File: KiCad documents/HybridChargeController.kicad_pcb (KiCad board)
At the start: 2 copper layers, 87 x 87 mm, 103 parts, among them P1 Load, P2 LI_balancer, P3 PV, P4 Extra, P5 LI, P6 LA, Q1 MMBT3904, Q10 MMBT3904, Q11 IPD90P04P4L-04, Q12 STL60P4LLF6, Q13 STL60P4LLF6, Q14 IPD90P04P4L-04, Q15 BSS138, Q16 BSS138, Q2 IPD90P04P4L-04, Q3 MMBT3904, Q4 IPD90P04P4L-04, Q5 IPD90P04P4L-04, Q6 MMBT3904, Q7 MMBT3904, Q8 MMBT3904, Q9 IPD90P04P4L-04, U1 LM358D, U2 bq76920, U3 cd4051, U4 LM358D, U5 LM358D

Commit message: switched 8 and 9 and hope for the best
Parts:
- added P7: FTDI, Pin_Headers:Pin_Header_Straight_1x06_Pitch2.54mm, F.Cu at (143.5, 137.1)
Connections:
- AU1 pad 8: /SW_PV -> /Alert
- AU1 pad 9: /Alert -> /SW_PV
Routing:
- net /SW_PV: track 15.1 -> 19.1 mm, vias 2 -> 3
- net /Alert: track 66.7 -> 70.2 mm, vias 5 -> 6
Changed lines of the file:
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@@
 (kicad_pcb (version 4) (host pcbnew 4.0.4-stable)
   (general
-    (links 252)
-    (no_connects 2)
-    (area 97 39 189.000001 129.000001)
+    (links 258)
+    (no_connects 8)
+    (area 99.924999 39.924999 187.075001 127.075001)
     (thickness 1.6)
     (drawings 58)
-    (tracks 882)
+    (tracks 893)
     (zones 0)
-    (modules 103)
+    (modules 104)
     (nets 92)
   )
@@
       (net 15 /SW_LD))
     (pad 8 thru_hole circle (at 41.656 -50.8 90) (size 1.7 1.7) (drill 1) (layers *.Cu *.Mask F.SilkS)
-      (net 68 /SW_PV))
-    (pad 9 thru_hole circle (at 39.116 -50.8 90) (size 1.7 1.7) (drill 1) (layers *.Cu *.Mask F.SilkS)
       (net 76 /Alert))
+    (pad 9 thru_hole circle (at 39.116 -50.8 90) (size 1.7 1.7) (drill 1) (layers *.Cu *.Mask F.SilkS)
+      (net 68 /SW_PV))
     (pad 10 thru_hole circle (at 36.576 -50.8 90) (size 1.7 1.7) (drill 1) (layers *.Cu *.Mask F.SilkS)
       (net 16 /SS))
@@
     )
   )
+  (module Pin_Headers:Pin_Header_Straight_1x06_Pitch2.54mm (layer F.Cu)
+    (at 143.5 137.075001)
+    (descr "Through hole straight pin header, 1x06, 2.54mm pitch, single row")
+    (tags "Through hole pin header THT 1x06 2.54mm single row")
+    (fp_text reference P7 (at 0 -2.33) (layer F.SilkS)
+      (effects (font (size 1 1) (thickness 0.15)))
+    )
+    (fp_text value FTDI (at 0 15.03) (layer F.Fab)
+      (effects (font (size 1 1) (thickness 0.15)))
+    )
+    (fp_line (start -1.27 -1.27) (end -1.27 13.97) (layer F.Fab) (width 0.1))
+    (fp_line (start -1.27 13.97) (end 1.27 13.97) (layer F.Fab) (width 0.1))
+    (fp_line (start 1.27 13.97) (end 1.27 -1.27) (layer F.Fab) (width 0.1))
+    (fp_line (start 1.27 -1.27) (end -1.27 -1.27) (layer F.Fab) (width 0.1))
+    (fp_line (start -1.33 1.27) (end -1.33 14.03) (layer F.SilkS) (width 0.12))
+    (fp_line (start -1.33 14.03) (end 1.33 14.03) (layer F.SilkS) (width 0.12))
+    (fp_line (start 1.33 14.03) (end 1.33 1.27) (layer F.SilkS) (width 0.12))
+    (fp_line (start 1.33 1.27) (end -1.33 1.27) (layer F.SilkS) (width 0.12))
+    (fp_line (start -1.33 0) (end -1.33 -1.33) (layer F.SilkS) (width 0.12))
+    (fp_line (start -1.33 -1.33) (end 0 -1.33) (layer F.SilkS) (width 0.12))
+    (fp_line (start -1.8 -1.8) (end -1.8 14.5) (layer F.CrtYd) (width 0.05))
+    (fp_line (start -1.8 14.5) (end 1.8 14.5) (layer F.CrtYd) (width 0.05))
+    (fp_line (start 1.8 14.5) (end 1.8 -1.8) (layer F.CrtYd) (width 0.05))
+    (fp_line (start 1.8 -1.8) (end -1.8 -1.8) (layer F.CrtYd) (width 0.05))
+    (fp_text user %R (at 0 -2.33) (layer F.Fab)
+      (effects (font (size 1 1) (thickness 0.15)))
+    )
+    (pad 1 thru_hole rect (at 0 0) (size 1.7 1.7) (drill 1) (layers *.Cu *.Mask)
+      (net 90 "Net-(P7-Pad1)"))
+    (pad 2 thru_hole oval (at 0 2.54) (size 1.7 1.7) (drill 1) (layers *.Cu *.Mask)
+      (net 9 /TX))
+    (pad 3 thru_hole oval (at 0 5.08) (size 1.7 1.7) (drill 1) (layers *.Cu *.Mask)
+      (net 8 /RX))
+    (pad 4 thru_hole oval (at 0 7.62) (size 1.7 1.7) (drill 1) (layers *.Cu *.Mask)
+      (net 21 /5V))
+    (pad 5 thru_hole oval (at 0 10.16) (size 1.7 1.7) (drill 1) (layers *.Cu *.Mask)
+      (net 91 "Net-(P7-Pad5)"))
+    (pad 6 thru_hole oval (at 0 12.7) (size 1.7 1.7) (drill 1) (layers *.Cu *.Mask)
+      (net 6 /GND))
+    (model ${KISYS3DMOD}/Pin_Headers.3dshapes/Pin_Header_Straight_1x06_Pitch2.54mm.wrl
+      (at (xyz 0 -0.25 0))
+      (scale (xyz 1 1 1))
+      (rotate (xyz 0 0 90))
+    )
+  )
   (gr_text X (at 176.25 79 90) (layer F.SilkS)
     (effects (font (size 0.75 0.75) (thickness 0.1)))
@@
   (segment (start 108.75 60.25) (end 109.365 59.635) (width 0.25) (layer F.Cu) (net 67))
   (segment (start 109.365 59.635) (end 109.365 58.825) (width 0.25) (layer F.Cu) (net 67))
-  (segment (start 165.1 71) (end 165 71) (width 0.25) (layer F.Cu) (net 68))
-  (segment (start 165 71) (end 164.25 71.75) (width 0.25) (layer F.Cu) (net 68))
-  (via (at 164.25 71.75) (size 0.6) (drill 0.4) (layers F.Cu B.Cu) (net 68))
-  (segment (start 164.25 71.75) (end 163.25 72.75) (width 0.25) (layer B.Cu) (net 68))
-  (segment (start 163.25 72.75) (end 163.25 73.25) (width 0.25) (layer B.Cu) (net 68))
-  (via (at 163.25 73.25) (size 0.6) (drill 0.4) (layers F.Cu B.Cu) (net 68))
-  (segment (start 163.25 73.25) (end 163.25 75.25) (width 0.25) (layer F.Cu) (net 68))
-  (segment (start 163.25 75.25) (end 161.25 77.25) (width 0.25) (layer F.Cu) (net 68))
+  (segment (start 158.276 77.25) (end 158.25 77.25) (width 0.25) (layer F.Cu) (net 68))
   (segment (start 161.25 77.25) (end 158.276 77.25) (width 0.25) (layer F.Cu) (net 68))
-  (segment (start 158.276 77.25) (end 155.321 74.295) (width 0.25) (layer F.Cu) (net 68))
+  (segment (start 163.25 75.25) (end 161.25 77.25) (width 0.25) (layer F.Cu) (net 68))
+  (segment (start 163.25 73.25) (end 163.25 75.25) (width 0.25) (layer F.Cu) (net 68))
+  (via (at 163.25 73.25) (size 0.6) (drill 0.4) (layers F.Cu B.Cu) (net 68))
+  (segment (start 163.25 72.75) (end 163.25 73.25) (width 0.25) (layer B.Cu) (net 68))
+  (segment (start 164.25 71.75) (end 163.25 72.75) (width 0.25) (layer B.Cu) (net 68))
+  (via (at 164.25 71.75) (size 0.6) (drill 0.4) (layers F.Cu B.Cu) (net 68))
+  (segment (start 165 71) (end 164.25 71.75) (width 0.25) (layer F.Cu) (net 68))
+  (segment (start 152.781 75.581) (end 152.781 74.295) (width 0.25) (layer B.Cu) (net 68))
+  (segment (start 153.7 76.5) (end 152.781 75.581) (width 0.25) (layer B.Cu) (net 68))
+  (segment (start 154.8 76.5) (end 153.7 76.5) (width 0.25) (layer B.Cu) (net 68))
+  (segment (start 155.7 75.6) (end 154.8 76.5) (width 0.25) (layer B.Cu) (net 68))
+  (segment (start 156.3 75.6) (end 155.7 75.6) (width 0.25) (layer B.Cu) (net 68))
+  (via (at 156.3 75.6) (size 0.6) (drill 0.4) (layers F.Cu B.Cu) (net 68))
+  (segment (start 156.6 75.6) (end 156.3 75.6) (width 0.25) (layer F.Cu) (net 68))
+  (segment (start 158.25 77.25) (end 156.6 75.6) (width 0.25) (layer F.Cu) (net 68))
+  (segment (start 165.1 71) (end 165 71) (width 0.25) (layer F.Cu) (net 68))
   (segment (start 166.825 96.425) (end 166.825 87.175) (width 0.25) (layer F.Cu) (net 69))
   (segment (start 169.5 68.75) (end 169.1 68.35) (width 0.25) (layer F.Cu) (net 69))
@@
   (segment (start 182.175 67.615) (end 184.015 67.615) (width 0.25) (layer F.Cu) (net 73))
   (segment (start 184.015 67.615) (end 185.25 68.85) (width 0.25) (layer F.Cu) (net 73))
-  (segment (start 152.781 74.295) (end 152.781 76.469) (width 0.25) (layer B.Cu) (net 76))
-  (segment (start 133.5 105.25) (end 138 100.75) (width 0.25) (layer F.Cu) (net 76))
-  (segment (start 138 100.75) (end 138 89.75) (width 0.25) (layer F.Cu) (net 76))
-  (via (at 138 89.75) (size 0.6) (drill 0.4) (layers F.Cu B.Cu) (net 76))
-  (segment (start 138 89.75) (end 138 85.5) (width 0.25) (layer B.Cu) (net 76))
-  (via (at 138 85.5) (size 0.6) (drill 0.4) (layers F.Cu B.Cu) (net 76))
-  (segment (start 119.183 117.433) (end 119.183 116.721) (width 0.25) (layer F.Cu) (net 76))
-  (segment (start 125.5 108.75) (end 129 105.25) (width 0.25) (layer F.Cu) (net 76))
-  (via (at 125.5 108.75) (size 0.6) (drill 0.4) (layers F.Cu B.Cu) (net 76))
-  (segment (start 125.5 111.25) (end 125.5 108.75) (width 0.25) (layer B.Cu) (net 76))
-  (segment (start 119.25 117.5) (end 125.5 111.25) (width 0.25) (layer B.Cu) (net 76))
-  (via (at 119.25 117.5) (size 0.6) (drill 0.4) (layers F.Cu B.Cu) (net 76))
-  (segment (start 119.183 117.433) (end 119.25 117.5) (width 0.25) (layer F.Cu) (net 76))
+  (segment (start 152 77.25) (end 155.25 77.25) (width 0.25) (layer B.Cu) (net 76))
   (segment (start 129 105.25) (end 133.5 105.25) (width 0.25) (layer F.Cu) (net 76))
-  (segment (start 138 80.75) (end 138 85.5) (width 0.25) (layer F.Cu) (net 76))
-  (segment (start 141.5 77.25) (end 138 80.75) (width 0.25) (layer F.Cu) (net 76))
-  (segment (start 152 77.25) (end 141.5 77.25) (width 0.25) (layer F.Cu) (net 76))
+  (segment (start 119.183 117.433) (end 119.25 117.5) (width 0.25) (layer F.Cu) (net 76))
+  (via (at 119.25 117.5) (size 0.6) (drill 0.4) (layers F.Cu B.Cu) (net 76))
+  (segment (start 119.25 117.5) (end 125.5 111.25) (width 0.25) (layer B.Cu) (net 76))
+  (segment (start 125.5 111.25) (end 125.5 108.75) (width 0.25) (layer B.Cu) (net 76))
+  (via (at 125.5 108.75) (size 0.6) (drill 0.4) (layers F.Cu B.Cu) (net 76))
+  (segment (start 125.5 108.75) (end 129 105.25) (width 0.25) (layer F.Cu) (net 76))
+  (segment (start 119.183 116.721) (end 119.183 117.433) (width 0.25) (layer F.Cu) (net 76))
+  (via (at 138 85.5) (size 0.6) (drill 0.4) (layers F.Cu B.Cu) (net 76))
+  (segment (start 138 89.75) (end 138 85.5) (width 0.25) (layer B.Cu) (net 76))
+  (via (at 138 89.75) (size 0.6) (drill 0.4) (layers F.Cu B.Cu) (net 76))
+  (segment (start 138 100.75) (end 138 89.75) (width 0.25) (layer F.Cu) (net 76))
+  (segment (start 133.5 105.25) (end 138 100.75) (width 0.25) (layer F.Cu) (net 76))
   (via (at 152 77.25) (size 0.6) (drill 0.4) (layers F.Cu B.Cu) (net 76))
-  (segment (start 152.781 76.469) (end 152 77.25) (width 0.25) (layer B.Cu) (net 76))
+  (segment (start 152 77.25) (end 141.5 77.25) (width 0.25) (layer F.Cu) (net 76))
+  (segment (start 141.5 77.25) (end 138 80.75) (width 0.25) (layer F.Cu) (net 76))
+  (segment (start 138 80.75) (end 138 85.5) (width 0.25) (layer F.Cu) (net 76))
+  (segment (start 155.321 75.821) (end 155.321 74.295) (width 0.25) (layer F.Cu) (net 76))
+  (segment (start 156 76.5) (end 155.321 75.821) (width 0.25) (layer F.Cu) (net 76))
+  (via (at 156 76.5) (size 0.6) (drill 0.4) (layers F.Cu B.Cu) (net 76))
+  (segment (start 155.25 77.25) (end 156 76.5) (width 0.25) (layer B.Cu) (net 76))
   (segment (start 120.1 89.73) (end 120.1 94.2) (width 0.25) (layer F.Cu) (net 80))
   (segment (start 120.1 94.2) (end 124 98.1) (width 0.25) (layer F.Cu) (net 80))

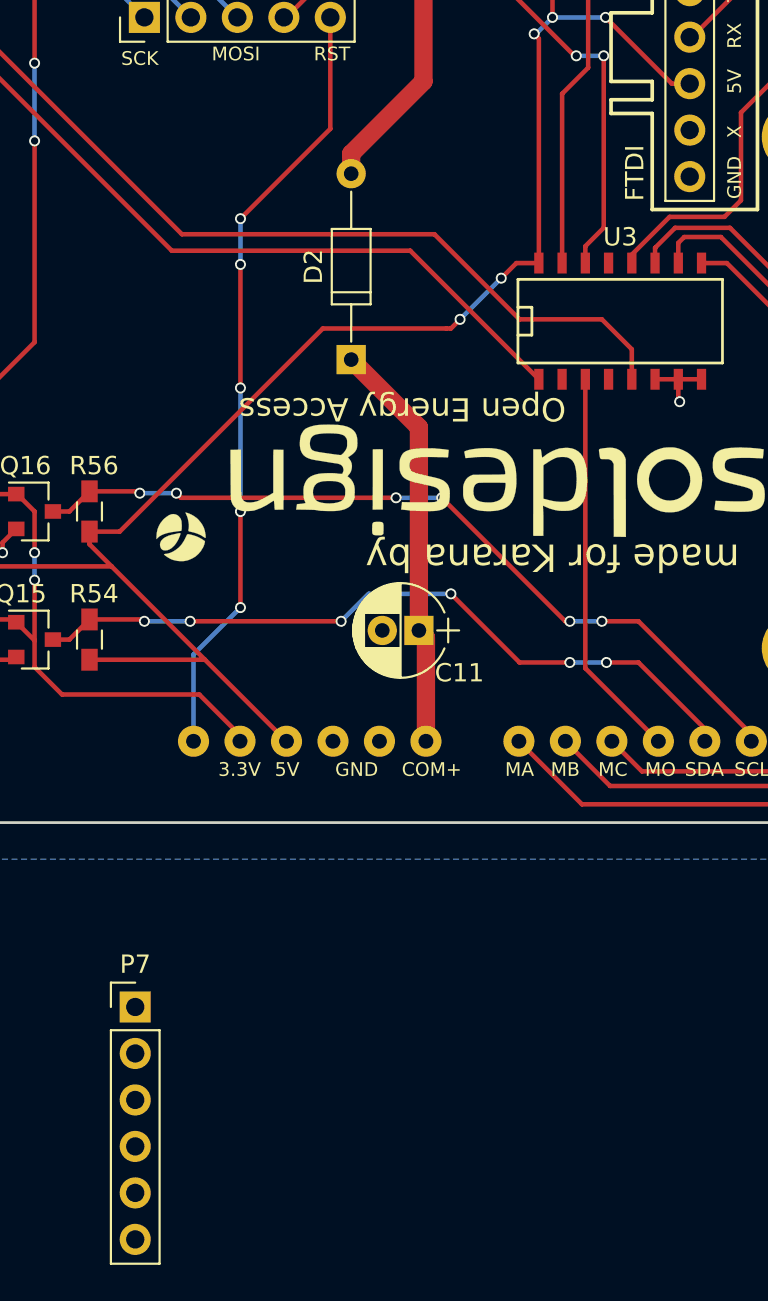
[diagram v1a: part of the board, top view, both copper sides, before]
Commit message: fixed extra holes, send new gerbers
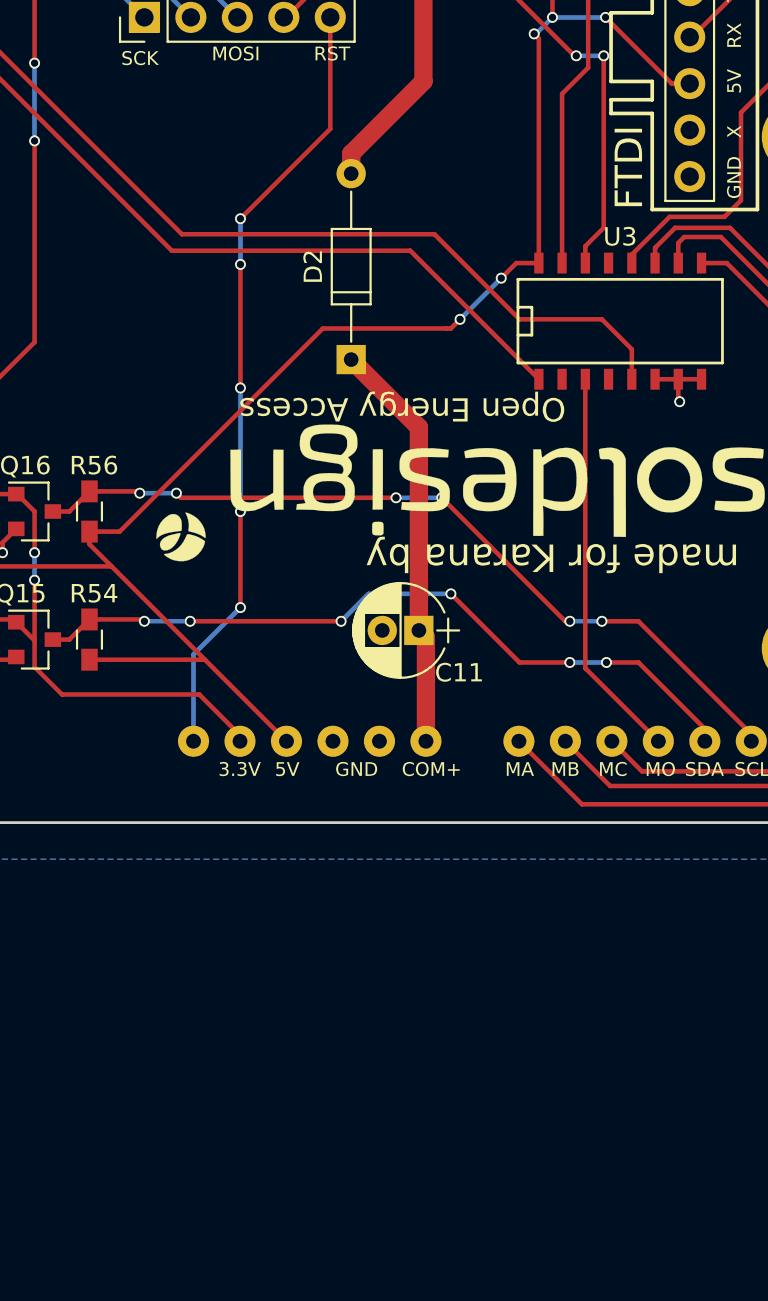
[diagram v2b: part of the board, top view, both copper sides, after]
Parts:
- removed the P7 at (143.5, 137.1)
- renumbered FTDI to P7
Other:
- board text added: "FTDI"
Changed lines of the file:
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@@
 (kicad_pcb (version 4) (host pcbnew 4.0.4-stable)
   (general
-    (links 258)
-    (no_connects 8)
+    (links 0)
+    (no_connects 2)
     (area 99.924999 39.924999 187.075001 127.075001)
     (thickness 1.6)
-    (drawings 58)
+    (drawings 59)
     (tracks 893)
     (zones 0)
-    (modules 104)
+    (modules 103)
     (nets 92)
   )
@@
     (descr "Through hole straight pin header, 1x06, 2.54mm pitch, single row")
     (tags "Through hole pin header THT 1x06 2.54mm single row")
-    (fp_text reference FTDI (at -3 12.5 90) (layer F.SilkS)
+    (fp_text reference P7 (at -3.1 2.3 90) (layer F.Fab)
       (effects (font (size 1 1) (thickness 0.15)))
     )
@@
     )
   )
-  (module Pin_Headers:Pin_Header_Straight_1x06_Pitch2.54mm (layer F.Cu)
-    (at 143.5 137.075001)
-    (descr "Through hole straight pin header, 1x06, 2.54mm pitch, single row")
-    (tags "Through hole pin header THT 1x06 2.54mm single row")
-    (fp_text reference P7 (at 0 -2.33) (layer F.SilkS)
-      (effects (font (size 1 1) (thickness 0.15)))
-    )
-    (fp_text value FTDI (at 0 15.03) (layer F.Fab)
-      (effects (font (size 1 1) (thickness 0.15)))
-    )
-    (fp_line (start -1.27 -1.27) (end -1.27 13.97) (layer F.Fab) (width 0.1))
-    (fp_line (start -1.27 13.97) (end 1.27 13.97) (layer F.Fab) (width 0.1))
-    (fp_line (start 1.27 13.97) (end 1.27 -1.27) (layer F.Fab) (width 0.1))
-    (fp_line (start 1.27 -1.27) (end -1.27 -1.27) (layer F.Fab) (width 0.1))
-    (fp_line (start -1.33 1.27) (end -1.33 14.03) (layer F.SilkS) (width 0.12))
-    (fp_line (start -1.33 14.03) (end 1.33 14.03) (layer F.SilkS) (width 0.12))
-    (fp_line (start 1.33 14.03) (end 1.33 1.27) (layer F.SilkS) (width 0.12))
-    (fp_line (start 1.33 1.27) (end -1.33 1.27) (layer F.SilkS) (width 0.12))
-    (fp_line (start -1.33 0) (end -1.33 -1.33) (layer F.SilkS) (width 0.12))
-    (fp_line (start -1.33 -1.33) (end 0 -1.33) (layer F.SilkS) (width 0.12))
-    (fp_line (start -1.8 -1.8) (end -1.8 14.5) (layer F.CrtYd) (width 0.05))
-    (fp_line (start -1.8 14.5) (end 1.8 14.5) (layer F.CrtYd) (width 0.05))
-    (fp_line (start 1.8 14.5) (end 1.8 -1.8) (layer F.CrtYd) (width 0.05))
-    (fp_line (start 1.8 -1.8) (end -1.8 -1.8) (layer F.CrtYd) (width 0.05))
-    (fp_text user %R (at 0 -2.33) (layer F.Fab)
-      (effects (font (size 1 1) (thickness 0.15)))
-    )
-    (pad 1 thru_hole rect (at 0 0) (size 1.7 1.7) (drill 1) (layers *.Cu *.Mask)
-      (net 90 "Net-(P7-Pad1)"))
-    (pad 2 thru_hole oval (at 0 2.54) (size 1.7 1.7) (drill 1) (layers *.Cu *.Mask)
-      (net 9 /TX))
-    (pad 3 thru_hole oval (at 0 5.08) (size 1.7 1.7) (drill 1) (layers *.Cu *.Mask)
-      (net 8 /RX))
-    (pad 4 thru_hole oval (at 0 7.62) (size 1.7 1.7) (drill 1) (layers *.Cu *.Mask)
-      (net 21 /5V))
-    (pad 5 thru_hole oval (at 0 10.16) (size 1.7 1.7) (drill 1) (layers *.Cu *.Mask)
-      (net 91 "Net-(P7-Pad5)"))
-    (pad 6 thru_hole oval (at 0 12.7) (size 1.7 1.7) (drill 1) (layers *.Cu *.Mask)
-      (net 6 /GND))
-    (model ${KISYS3DMOD}/Pin_Headers.3dshapes/Pin_Header_Straight_1x06_Pitch2.54mm.wrl
-      (at (xyz 0 -0.25 0))
-      (scale (xyz 1 1 1))
-      (rotate (xyz 0 0 90))
-    )
+  (gr_text FTDI (at 170.5 91.2 90) (layer F.SilkS)
+    (effects (font (size 1.5 1.5) (thickness 0.2)))
   )
   (gr_text X (at 176.25 79 90) (layer F.SilkS)

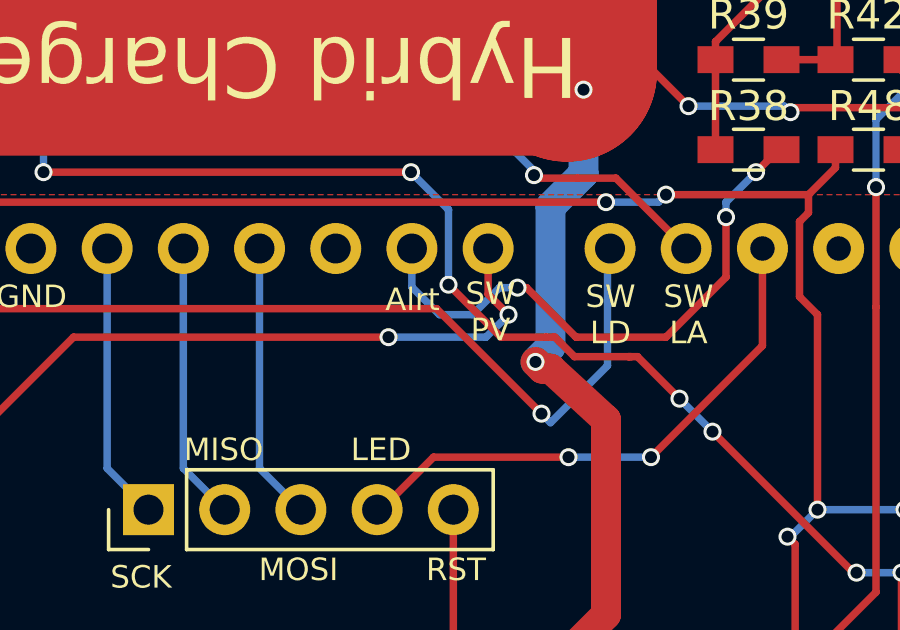
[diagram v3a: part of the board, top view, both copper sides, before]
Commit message: will alter PI controller into struct
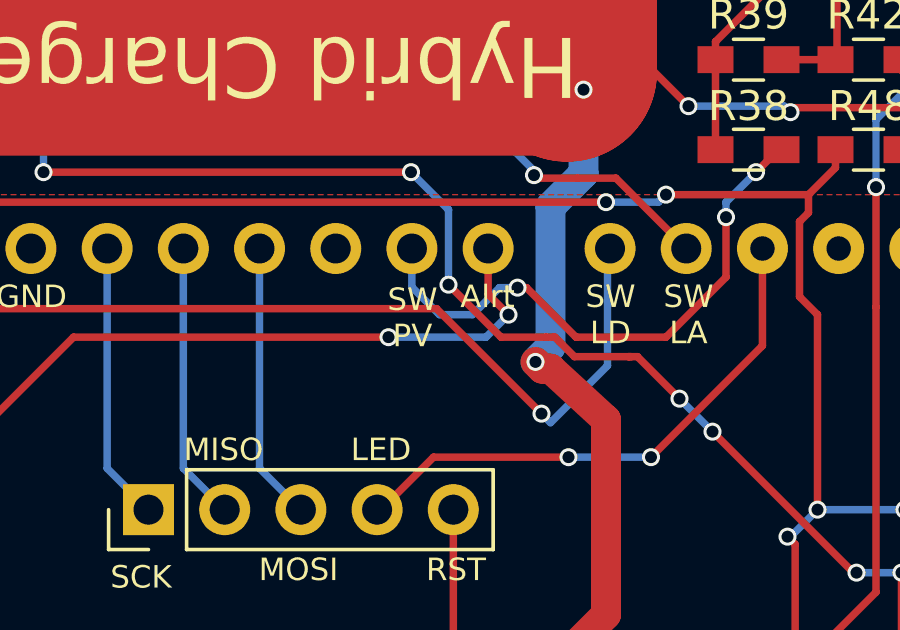
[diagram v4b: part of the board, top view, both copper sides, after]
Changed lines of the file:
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@@
       (padsonsilk false)
       (subtractmaskfromsilk false)
-      (outputformat 1)
+      (outputformat 4)
       (mirror false)
       (drillshape 0)
@@
     (effects (font (size 0.75 0.75) (thickness 0.1)))
   )
-  (gr_text Alrt (at 152.8 76) (layer F.SilkS)
+  (gr_text Alrt (at 155.3 75.9) (layer F.SilkS)
     (effects (font (size 0.75 0.75) (thickness 0.1)))
   )
-  (gr_text "SW\nPV" (at 155.4 76.4) (layer F.SilkS)
+  (gr_text "SW\nPV" (at 152.8 76.6) (layer F.SilkS)
     (effects (font (size 0.75 0.75) (thickness 0.1)))
   )
